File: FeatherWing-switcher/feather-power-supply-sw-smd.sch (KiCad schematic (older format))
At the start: 24 parts, among them J1 5.08mm, J2 Conn_01x12, J3 Conn_01x16, U1 TPS5405DR

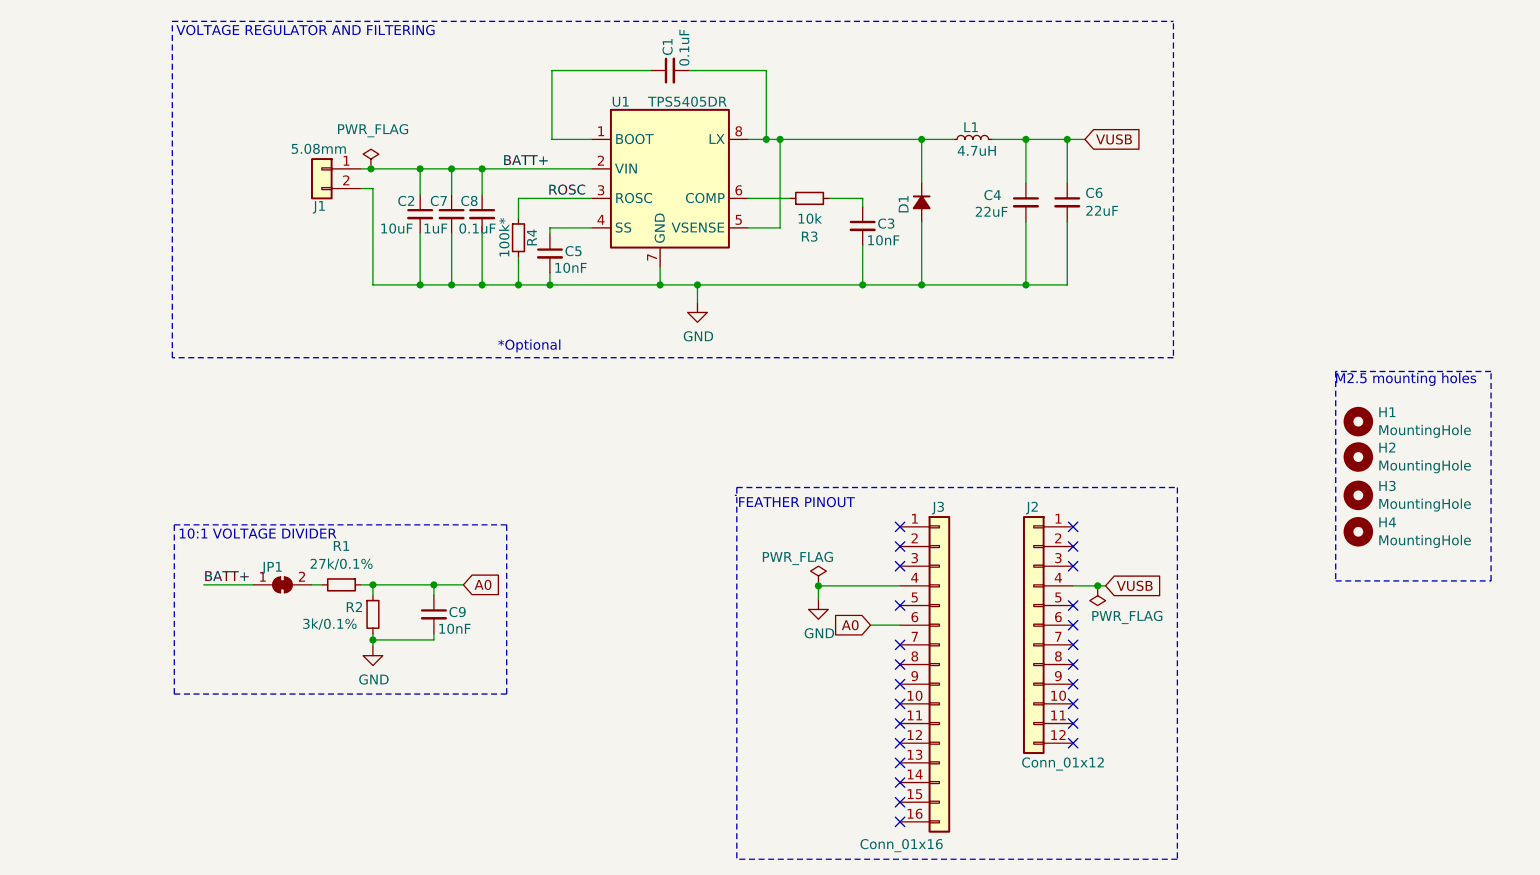
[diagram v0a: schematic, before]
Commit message: adds oshw logo; fixes a0 pin ref
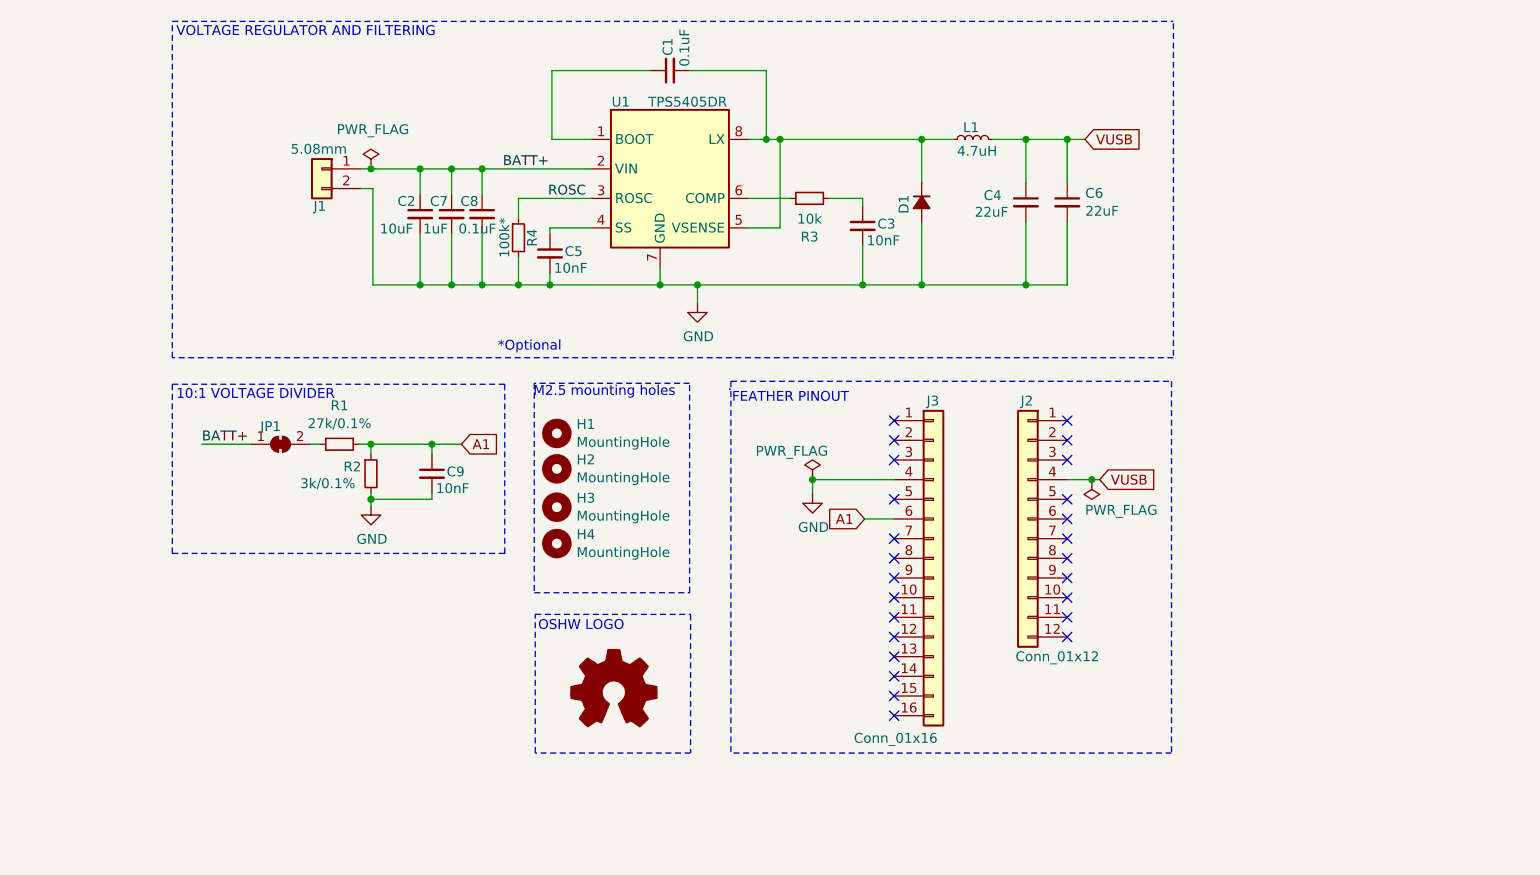
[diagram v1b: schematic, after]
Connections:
- net A0 renamed A1
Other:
- note added: "OSHW LOGO"
- moved on the sheet: C9, H1, H2, H3, H4, J2, J3, JP1, R1, R2

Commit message: update mounting holes
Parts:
- removed H1, H2: MountingHole, MountingHole:MountingHole_2.7mm_M2.5, symbol Mechanical:MountingHole
- added H1, H2: MountingHole_Pad, MountingHole:MountingHole_2.5mm_Pad, symbol Mechanical:MountingHole_Pad
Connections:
- net GND: now also H1.1, H2.1
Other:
- moved on the sheet: H3, H4
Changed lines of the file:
@@
 $EndComp
 Connection ~ 6325 3900
-Text Label 3220 3720 0    50   ~ 0
+Text Label 3220 3710 0    50   ~ 0
 BATT+
-Text GLabel 4540 3720 2    50   Input ~ 0
+Text GLabel 4540 3710 2    50   Input ~ 0
 A1
 Text GLabel 6590 4100 0    50   Input ~ 0
@@
 	5910 3400 5910 5290
 Wire Notes Line
-	4760 3415 4760 4275
+	4760 3405 4760 4265
 Wire Notes Line
 	8160 1580 8160 3280
@@
 Wire Wire Line
 	4490 2910 4645 2910
-$Comp
-L Mechanical:MountingHole H1
-U 1 1 5F4DCA7B
-P 5025 3665
-F 0 "H1" H 5125 3711 50  0000 L CNN
-F 1 "MountingHole" H 5125 3620 50  0000 L CNN
-F 2 "MountingHole:MountingHole_2.7mm_M2.5" H 5025 3665 50  0001 C CNN
-F 3 "~" H 5025 3665 50  0001 C CNN
-	1    5025 3665
-	1    0    0    -1
-$EndComp
-$Comp
-L Mechanical:MountingHole H2
-U 1 1 5F4E3BF8
-P 5025 3845
-F 0 "H2" H 5125 3891 50  0000 L CNN
-F 1 "MountingHole" H 5125 3800 50  0000 L CNN
-F 2 "MountingHole:MountingHole_2.7mm_M2.5" H 5025 3845 50  0001 C CNN
-F 3 "~" H 5025 3845 50  0001 C CNN
-	1    5025 3845
-	1    0    0    -1
-$EndComp
-$Comp
-L Mechanical:MountingHole H3
-U 1 1 5F4E3ED4
-P 5025 4040
-F 0 "H3" H 5125 4086 50  0000 L CNN
-F 1 "MountingHole" H 5125 3995 50  0000 L CNN
-F 2 "MountingHole:MountingHole_2.7mm_M2.5" H 5025 4040 50  0001 C CNN
-F 3 "~" H 5025 4040 50  0001 C CNN
-	1    5025 4040
-	1    0    0    -1
-$EndComp
-$Comp
-L Mechanical:MountingHole H4
-U 1 1 5F4E4234
-P 5025 4225
-F 0 "H4" H 5125 4271 50  0000 L CNN
-F 1 "MountingHole" H 5125 4180 50  0000 L CNN
-F 2 "MountingHole:MountingHole_2.7mm_M2.5" H 5025 4225 50  0001 C CNN
-F 3 "~" H 5025 4225 50  0001 C CNN
-	1    5025 4225
-	1    0    0    -1
-$EndComp
-Wire Notes Line
-	4910 4475 5700 4475
-Wire Notes Line
-	5700 4475 5700 3410
-Wire Notes Line
-	5700 3410 4910 3410
-Wire Notes Line
-	4910 3410 4910 4475
-Text Notes 4905 3485 0    50   ~ 0
+Text Notes 4935 3475 0    50   ~ 0
 M2.5 mounting holes
 Wire Wire Line
-	3220 3720 3470 3720
-Wire Notes Line
-	3070 4275 4760 4275
-Wire Notes Line
-	3070 3415 4760 3415
-Wire Notes Line
-	3070 3415 3070 4280
+	3220 3710 3470 3710
+Wire Notes Line
+	3070 4265 4760 4265
+Wire Notes Line
+	3070 3405 4760 3405
+Wire Notes Line
+	3070 3405 3070 4270
 $Comp
 L Jumper:SolderJumper_2_Bridged JP1
 U 1 1 5F4E9F72
-P 3620 3720
-F 0 "JP1" H 3570 3810 50  0000 C CNN
-F 1 "SolderJumper_2_Bridged" H 3285 3630 50  0001 C CNN
-F 2 "Jumper:SolderJumper-2_P1.3mm_Bridged_RoundedPad1.0x1.5mm" H 3620 3720 50  0001 C CNN
-F 3 "~" H 3620 3720 50  0001 C CNN
-	1    3620 3720
-	1    0    0    -1
-$EndComp
-Text Notes 3090 3500 0    50   ~ 0
+P 3620 3710
+F 0 "JP1" H 3570 3800 50  0000 C CNN
+F 1 "SolderJumper_2_Bridged" H 3285 3620 50  0001 C CNN
+F 2 "Jumper:SolderJumper-2_P1.3mm_Bridged_RoundedPad1.0x1.5mm" H 3620 3710 50  0001 C CNN
+F 3 "~" H 3620 3710 50  0001 C CNN
+	1    3620 3710
+	1    0    0    -1
+$EndComp
+Text Notes 3090 3490 0    50   ~ 0
 10:1 VOLTAGE DIVIDER
 Wire Wire Line
-	4080 4030 4080 4000
-Wire Wire Line
-	4080 3720 4080 3770
+	4080 4020 4080 3990
+Wire Wire Line
+	4080 3710 4080 3760
 $Comp
 L power:GND #PWR02
 U 1 1 5F4755CE
-P 4080 4030
-F 0 "#PWR02" H 4080 3780 50  0001 C CNN
-F 1 "GND" H 4085 3857 50  0000 C CNN
-F 2 "" H 4080 4030 50  0001 C CNN
-F 3 "" H 4080 4030 50  0001 C CNN
-	1    4080 4030
+P 4080 4020
+F 0 "#PWR02" H 4080 3770 50  0001 C CNN
+F 1 "GND" H 4085 3847 50  0000 C CNN
+F 2 "" H 4080 4020 50  0001 C CNN
+F 3 "" H 4080 4020 50  0001 C CNN
+	1    4080 4020
 	1    0    0    -1
 $EndComp
@@
 L Device:R_Small R1
 U 1 1 5F47540B
-P 3920 3720
-F 0 "R1" V 3724 3720 50  0000 C CNN
-F 1 "27k/0.1%" V 3815 3720 50  0000 C CNN
-F 2 "Resistor_SMD:R_0603_1608Metric_Pad1.05x0.95mm_HandSolder" H 3920 3720 50  0001 C CNN
-F 3 "~" H 3920 3720 50  0001 C CNN
-F 4 "‎P20138CT-ND‎" V 3920 3720 50  0001 C CNN "DigiKey_PN"
-	1    3920 3720
+P 3920 3710
+F 0 "R1" V 3724 3710 50  0000 C CNN
+F 1 "27k/0.1%" V 3815 3710 50  0000 C CNN
+F 2 "Resistor_SMD:R_0603_1608Metric_Pad1.05x0.95mm_HandSolder" H 3920 3710 50  0001 C CNN
+F 3 "~" H 3920 3710 50  0001 C CNN
+F 4 "‎P20138CT-ND‎" V 3920 3710 50  0001 C CNN "DigiKey_PN"
+	1    3920 3710
 	0    1    1    0
 $EndComp
@@
 L Device:R_Small R2
 U 1 1 5F475325
-P 4080 3870
-F 0 "R2" H 3940 3905 50  0000 L CNN
-F 1 "3k/0.1%" H 3720 3820 50  0000 L CNN
-F 2 "Resistor_SMD:R_0603_1608Metric_Pad1.05x0.95mm_HandSolder" H 4080 3870 50  0001 C CNN
-F 3 "~" H 4080 3870 50  0001 C CNN
-F 4 "P20072CT-ND‎" H 4080 3870 50  0001 C CNN "DigiKey_PN"
-	1    4080 3870
+P 4080 3860
+F 0 "R2" H 3940 3895 50  0000 L CNN
+F 1 "3k/0.1%" H 3720 3810 50  0000 L CNN
+F 2 "Resistor_SMD:R_0603_1608Metric_Pad1.05x0.95mm_HandSolder" H 4080 3860 50  0001 C CNN
+F 3 "~" H 4080 3860 50  0001 C CNN
+F 4 "P20072CT-ND‎" H 4080 3860 50  0001 C CNN "DigiKey_PN"
+	1    4080 3860
 	1    0    0    -1
 $EndComp
@@
 $EndComp
 Wire Wire Line
-	3770 3720 3820 3720
+	3770 3710 3820 3710
 $Comp
 L Device:C_Small C9
 U 1 1 5F52B2E4
-P 4390 3870
-F 0 "C9" H 4465 3880 50  0000 L CNN
-F 1 "10nF" H 4410 3795 50  0000 L CNN
-F 2 "Capacitor_SMD:C_0603_1608Metric_Pad1.05x0.95mm_HandSolder" H 4390 3870 50  0001 C CNN
-F 3 "~" H 4390 3870 50  0001 C CNN
-	1    4390 3870
-	1    0    0    -1
-$EndComp
-Wire Wire Line
-	4540 3720 4390 3720
-Connection ~ 4080 3720
-Wire Wire Line
-	4080 3720 4020 3720
-Wire Wire Line
-	4390 3770 4390 3720
-Connection ~ 4390 3720
-Wire Wire Line
-	4390 3720 4080 3720
-Wire Wire Line
-	4390 3970 4390 4000
-Wire Wire Line
-	4390 4000 4080 4000
-Connection ~ 4080 4000
-Wire Wire Line
-	4080 4000 4080 3970
-$Comp
-L Graphic:Logo_Open_Hardware_Small #LOGO?
+P 4390 3860
+F 0 "C9" H 4465 3870 50  0000 L CNN
+F 1 "10nF" H 4410 3785 50  0000 L CNN
+F 2 "Capacitor_SMD:C_0603_1608Metric_Pad1.05x0.95mm_HandSolder" H 4390 3860 50  0001 C CNN
+F 3 "~" H 4390 3860 50  0001 C CNN
+	1    4390 3860
+	1    0    0    -1
+$EndComp
+Wire Wire Line
+	4540 3710 4390 3710
+Connection ~ 4080 3710
+Wire Wire Line
+	4080 3710 4020 3710
+Wire Wire Line
+	4390 3760 4390 3710
+Connection ~ 4390 3710
+Wire Wire Line
+	4390 3710 4080 3710
+Wire Wire Line
+	4390 3960 4390 3990
+Wire Wire Line
+	4390 3990 4080 3990
+Connection ~ 4080 3990
+Wire Wire Line
+	4080 3990 4080 3960
+$Comp
+L Graphic:Logo_Open_Hardware_Small #LOGO1
 U 1 1 5F51AA5B
-P 5315 4985
-F 0 "#LOGO?" H 5315 5260 50  0001 C CNN
-F 1 "Logo_Open_Hardware_Small" H 5315 4760 50  0001 C CNN
-F 2 "Symbol:OSHW-Logo2_7.3x6mm_Copper" H 5315 4985 50  0001 C CNN
-F 3 "~" H 5315 4985 50  0001 C CNN
-	1    5315 4985
-	1    0    0    -1
-$EndComp
-Wire Notes Line
-	5705 5290 4915 5290
-Wire Notes Line
-	4915 5290 4915 4585
-Wire Notes Line
-	4915 4585 5705 4585
-Wire Notes Line
-	5705 4585 5705 5290
-Text Notes 4930 4675 0    50   ~ 0
+P 5340 4985
+F 0 "#LOGO1" H 5340 5260 50  0001 C CNN
+F 1 "Logo_Open_Hardware_Small" H 5340 4760 50  0001 C CNN
+F 2 "Symbol:OSHW-Logo2_7.3x6mm_Copper" H 5340 4985 50  0001 C CNN
+F 3 "~" H 5340 4985 50  0001 C CNN
+	1    5340 4985
+	1    0    0    -1
+$EndComp
+Wire Notes Line
+	5730 5290 4940 5290
+Wire Notes Line
+	4940 5290 4940 4585
+Wire Notes Line
+	4940 4585 5730 4585
+Wire Notes Line
+	5730 4585 5730 5290
+Text Notes 4955 4675 0    50   ~ 0
 OSHW LOGO
+$Comp
+L Mechanical:MountingHole H4
+U 1 1 5F4E4234
+P 4995 4430
+F 0 "H4" H 5095 4476 50  0000 L CNN
+F 1 "MountingHole" H 5095 4385 50  0000 L CNN
+F 2 "MountingHole:MountingHole_2.7mm_M2.5" H 4995 4430 50  0001 C CNN
+F 3 "~" H 4995 4430 50  0001 C CNN
+	1    4995 4430
+	1    0    0    -1
+$EndComp
+$Comp
+L Mechanical:MountingHole_Pad H1
+U 1 1 5F541A68
+P 4995 3610
+F 0 "H1" H 5095 3659 50  0000 L CNN
+F 1 "MountingHole_Pad" H 5095 3568 50  0000 L CNN
+F 2 "MountingHole:MountingHole_2.5mm_Pad" H 4995 3610 50  0001 C CNN
+F 3 "~" H 4995 3610 50  0001 C CNN
+	1    4995 3610
+	1    0    0    -1
+$EndComp
+$Comp
+L Mechanical:MountingHole H3
+U 1 1 5F4E3ED4
+P 4990 4250
+F 0 "H3" H 5090 4296 50  0000 L CNN
+F 1 "MountingHole" H 5090 4205 50  0000 L CNN
+F 2 "MountingHole:MountingHole_2.7mm_M2.5" H 4990 4250 50  0001 C CNN
+F 3 "~" H 4990 4250 50  0001 C CNN
+	1    4990 4250
+	1    0    0    -1
+$EndComp
+$Comp
+L Mechanical:MountingHole_Pad H2
+U 1 1 5F54DC92
+P 5000 3955
+F 0 "H2" H 5100 4004 50  0000 L CNN
+F 1 "MountingHole_Pad" H 5100 3913 50  0000 L CNN
+F 2 "MountingHole:MountingHole_2.5mm_Pad" H 5000 3955 50  0001 C CNN
+F 3 "~" H 5000 3955 50  0001 C CNN
+	1    5000 3955
+	1    0    0    -1
+$EndComp
+$Comp
+L power:GND #PWR04
+U 1 1 5F54E691
+P 4995 3710
+F 0 "#PWR04" H 4995 3460 50  0001 C CNN
+F 1 "GND" H 5135 3640 50  0000 C CNN
+F 2 "" H 4995 3710 50  0001 C CNN
+F 3 "" H 4995 3710 50  0001 C CNN
+	1    4995 3710
+	1    0    0    -1
+$EndComp
+$Comp
+L power:GND #PWR05
+U 1 1 5F55451D
+P 5000 4055
+F 0 "#PWR05" H 5000 3805 50  0001 C CNN
+F 1 "GND" H 5135 4025 50  0000 C CNN
+F 2 "" H 5000 4055 50  0001 C CNN
+F 3 "" H 5000 4055 50  0001 C CNN
+	1    5000 4055
+	1    0    0    -1
+$EndComp
+Wire Notes Line
+	4880 4535 5795 4535
+Wire Notes Line
+	5795 4535 5795 3400
+Wire Notes Line
+	4880 3400 5795 3400
+Wire Notes Line
+	4880 3400 4880 4535
 $EndSCHEMATC

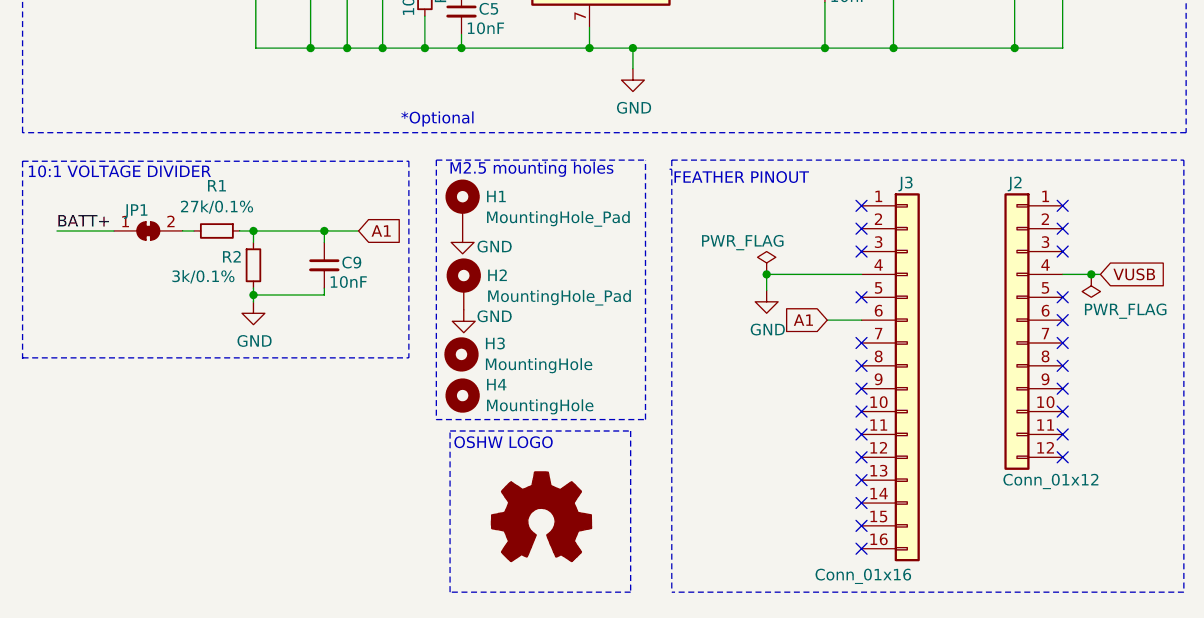
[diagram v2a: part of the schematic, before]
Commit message: adds qwicc conn
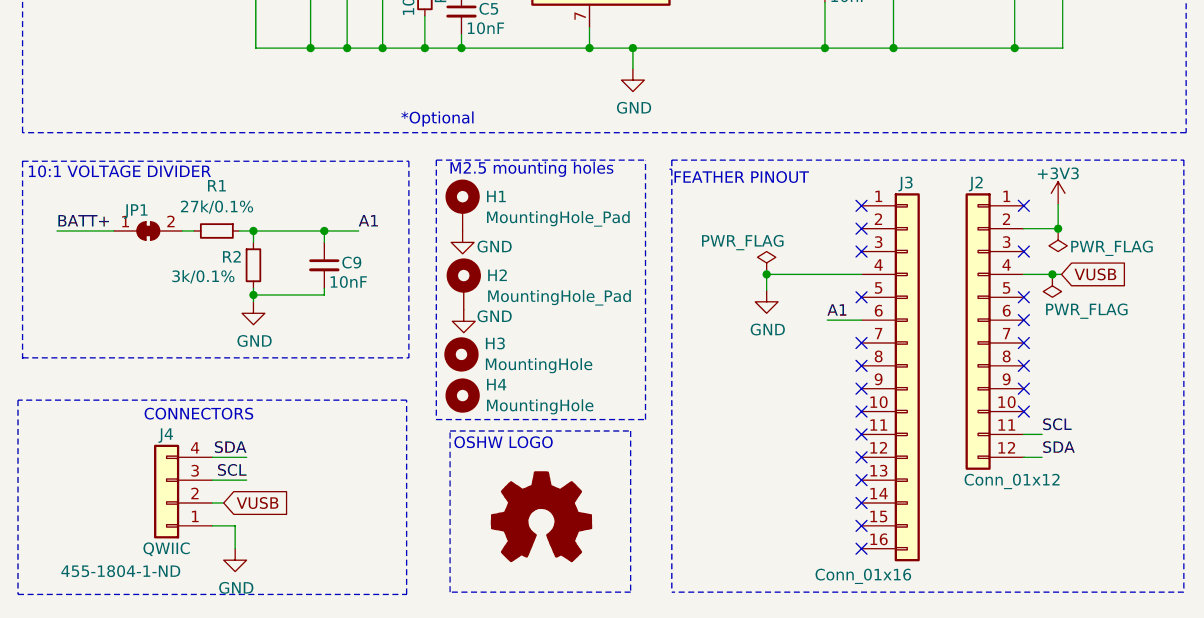
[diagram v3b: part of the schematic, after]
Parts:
- added J4: QWIIC, Connector_JST:JST_SH_SM04B-SRSS-TB_1x04-1MP_P1.00mm_Horizontal, symbol Connector_Generic:Conn_01x04
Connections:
- net GND: now also J4.1 (Pin_1)
- net VUSB: now also J4.2 (Pin_2)
- net SCL: now reaches J2.11 (Pin_11)
- net SCL: now also J4.3 (Pin_3)
- net SDA: now reaches J2.12 (Pin_12)
- net SDA: now also J4.4 (Pin_4)
- net +3V3: now reaches J2.2 (Pin_2)
- no-connect marks 25 -> 22
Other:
- note added: "CONNECTORS"
- moved on the sheet: J2
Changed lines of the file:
@@
 L Connector_Generic:Conn_01x12 J2
 U 1 1 5F4351FA
-P 7420 4100
-F 0 "J2" H 7425 4700 50  0000 C CNN
-F 1 "Conn_01x12" H 7270 3400 50  0000 C CNN
-F 2 "Connector_PinHeader_2.54mm:PinHeader_1x12_P2.54mm_Vertical" H 7420 4100 50  0001 C CNN
-F 3 "~" H 7420 4100 50  0001 C CNN
-	1    7420 4100
+P 7250 4100
+F 0 "J2" H 7255 4700 50  0000 C CNN
+F 1 "Conn_01x12" H 7100 3400 50  0000 C CNN
+F 2 "Connector_PinHeader_2.54mm:PinHeader_1x12_P2.54mm_Vertical" H 7250 4100 50  0001 C CNN
+F 3 "~" H 7250 4100 50  0001 C CNN
+	1    7250 4100
 	-1   0    0    -1
 $EndComp
@@
 	1    0    0    -1
 $EndComp
-Text GLabel 7785 3900 2    50   Input ~ 0
+Text GLabel 7615 3900 2    50   Input ~ 0
 VUSB
 Wire Wire Line
-	7620 3900 7745 3900
+	7450 3900 7575 3900
 $Comp
 L power:GND #PWR03
@@
 L power:PWR_FLAG #FLG02
 U 1 1 5F43E163
-P 7745 3900
-F 0 "#FLG02" H 7745 3975 50  0001 C CNN
-F 1 "PWR_FLAG" H 7595 4055 50  0000 C CNN
-F 2 "" H 7745 3900 50  0001 C CNN
-F 3 "~" H 7745 3900 50  0001 C CNN
-	1    7745 3900
+P 7575 3900
+F 0 "#FLG02" H 7575 3975 50  0001 C CNN
+F 1 "PWR_FLAG" H 7425 4055 50  0000 C CNN
+F 2 "" H 7575 3900 50  0001 C CNN
+F 3 "~" H 7575 3900 50  0001 C CNN
+	1    7575 3900
 	-1   0    0    1
 $EndComp
-Connection ~ 7745 3900
-Wire Wire Line
-	7745 3900 7785 3900
+Connection ~ 7575 3900
+Wire Wire Line
+	7575 3900 7615 3900
 $Comp
 L power:PWR_FLAG #FLG01
@@
 Text Label 3220 3710 0    50   ~ 0
 BATT+
-Text GLabel 4540 3710 2    50   Input ~ 0
-A1
-Text GLabel 6590 4100 0    50   Input ~ 0
-A1
 Wire Wire Line
 	6590 4100 6740 4100
-NoConn ~ 7620 3700
-NoConn ~ 7620 3800
-NoConn ~ 7620 4000
-NoConn ~ 7620 4100
-NoConn ~ 7620 4200
-NoConn ~ 7620 4300
-NoConn ~ 7620 4400
-NoConn ~ 7620 4500
-NoConn ~ 7620 4600
-NoConn ~ 7620 4700
+NoConn ~ 7450 3800
+NoConn ~ 7450 4000
+NoConn ~ 7450 4100
+NoConn ~ 7450 4200
+NoConn ~ 7450 4300
+NoConn ~ 7450 4400
+NoConn ~ 7450 4500
 NoConn ~ 6740 3700
 NoConn ~ 6740 3800
@@
 Text Label 4980 2470 0    50   ~ 0
 ROSC
-NoConn ~ 7620 3600
+NoConn ~ 7450 3600
 NoConn ~ 6740 3600
 Wire Notes Line
@@
 Wire Notes Line
 	4880 3400 4880 4535
+$Comp
+L Connector_Generic:Conn_01x04 J4
+U 1 1 5F572FDE
+P 3700 4900
+F 0 "J4" H 3700 4600 50  0000 C CNN
+F 1 "QWIIC" H 3700 5100 50  0000 C CNN
+F 2 "Connector_JST:JST_SH_SM04B-SRSS-TB_1x04-1MP_P1.00mm_Horizontal" H 3700 4900 50  0001 C CNN
+F 3 "https://cdn-shop.adafruit.com/product-files/4328/4328_C13916-001_CCSH-W10-04-BK-RC-A.pdf" H 3700 4900 50  0001 C CNN
+F 4 "455-1804-1-ND" H 3900 5200 50  0000 C CNN "DigiKey_PN"
+	1    3700 4900
+	-1   0    0    1
+$EndComp
+$Comp
+L power:GND #PWR08
+U 1 1 5F5932C7
+P 4000 5100
+F 0 "#PWR08" H 4000 4850 50  0001 C CNN
+F 1 "GND" H 4005 4927 50  0000 C CNN
+F 2 "" H 4000 5100 50  0001 C CNN
+F 3 "" H 4000 5100 50  0001 C CNN
+	1    4000 5100
+	1    0    0    -1
+$EndComp
+Wire Wire Line
+	3900 5000 4000 5000
+Wire Wire Line
+	4000 5000 4000 5100
+$Comp
+L power:+3V3 #PWR06
+U 1 1 5F59A739
+P 7600 3595
+F 0 "#PWR06" H 7600 3445 50  0001 C CNN
+F 1 "+3V3" H 7600 3730 50  0000 C CNN
+F 2 "" H 7600 3595 50  0001 C CNN
+F 3 "" H 7600 3595 50  0001 C CNN
+	1    7600 3595
+	1    0    0    -1
+$EndComp
+Wire Wire Line
+	7450 3700 7600 3700
+Wire Wire Line
+	7600 3700 7600 3595
+$Comp
+L power:PWR_FLAG #FLG04
+U 1 1 5F5B29C7
+P 7600 3700
+F 0 "#FLG04" H 7600 3775 50  0001 C CNN
+F 1 "PWR_FLAG" H 7365 3780 50  0000 C CNN
+F 2 "" H 7600 3700 50  0001 C CNN
+F 3 "~" H 7600 3700 50  0001 C CNN
+	1    7600 3700
+	-1   0    0    1
+$EndComp
+Connection ~ 7600 3700
+Text Label 4540 3710 0    50   ~ 0
+A1
+Text Label 6590 4100 0    50   ~ 0
+A1
+Wire Wire Line
+	7450 4700 7530 4700
+Wire Wire Line
+	7450 4600 7530 4600
+Text Label 7530 4700 0    50   ~ 0
+SDA
+Text Label 7530 4600 0    50   ~ 0
+SCL
+Wire Wire Line
+	3900 4700 4050 4700
+Wire Wire Line
+	3900 4800 4050 4800
+Text Label 4050 4700 2    50   ~ 0
+SDA
+Text Label 4050 4800 2    50   ~ 0
+SCL
+Text GLabel 3950 4900 2    50   Input ~ 0
+VUSB
+Wire Wire Line
+	3900 4900 3950 4900
+Wire Notes Line
+	3050 4450 3050 5300
+Wire Notes Line
+	4750 5300 4750 4450
+Wire Notes Line
+	4750 4450 3050 4450
+Text Notes 3600 4550 0    50   ~ 0
+CONNECTORS
+Wire Notes Line
+	3050 5300 4750 5300
 $EndSCHEMATC
